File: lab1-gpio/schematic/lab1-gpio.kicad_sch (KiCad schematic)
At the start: 9 parts

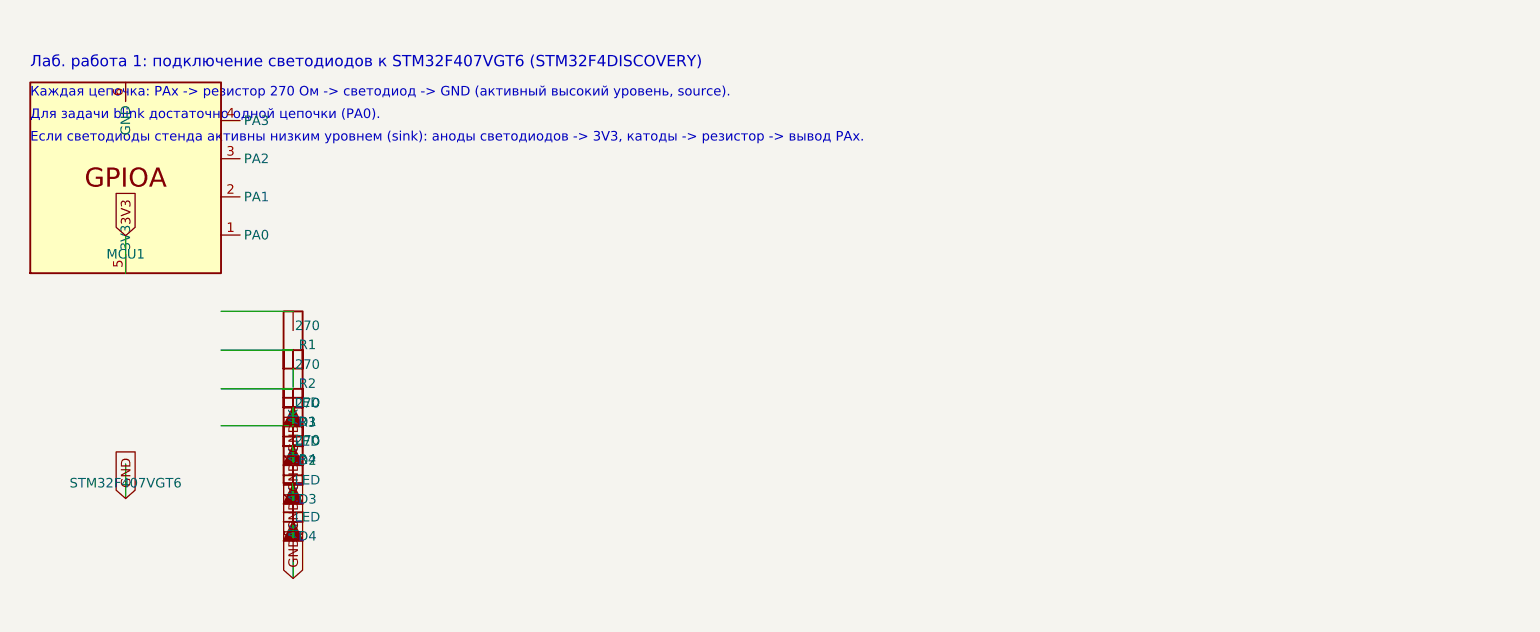
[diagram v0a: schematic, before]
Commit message: Lab 1: fix schema, add validator
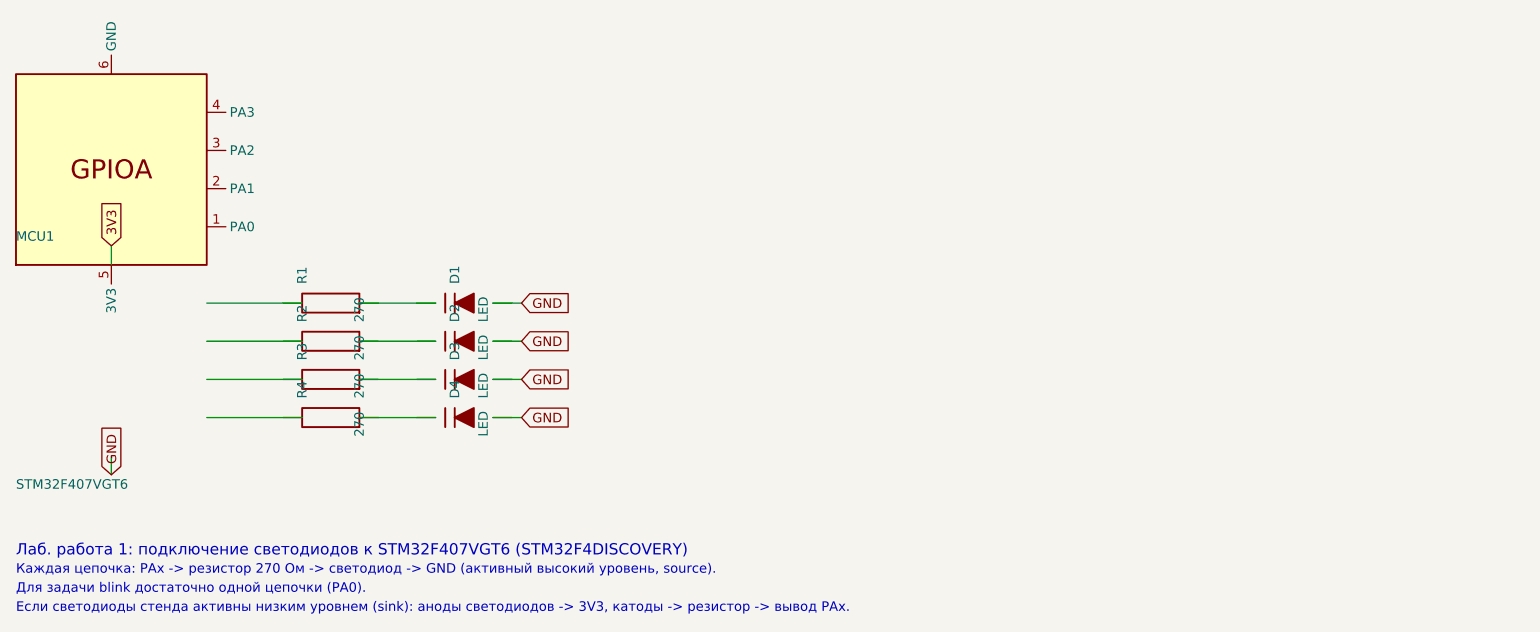
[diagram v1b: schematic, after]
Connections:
- net GND: no longer D4.2 (K), R3.1, R4.1
- net at R1.1: now also D1.2 (K)
- net at R2.1: now also D2.2 (K); no longer R4.2
- net at D3.2 (K): now also R3.1
- new net: D4.2 (K), R4.1
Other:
- moved on the sheet: MCU1, R1, R2, R3, R4
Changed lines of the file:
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@@
     (title "Лаб. работа 1: подключение светодиодов к STM32F407VGT6")
     (date "2026-09-12")
-    (rev "1.0")
+    (rev "1.1")
   )
-  ; ============ MCU ============
-  (symbol (lib_id "Lab:STM32F407_GPIO") (at 40 90 0)
+  (symbol (lib_id "Lab:STM32F407_GPIO") (at 38.1 88.9 0)
     (unit 1)
     (in_bom yes) (on_board yes)
-    (property "Reference" "MCU1" (at 52.7 87.46 0) (effects (font (size 1.27 1.27))))
-    (property "Value" "STM32F407VGT6" (at 52.7 117.94 0) (effects (font (size 1.27 1.27))))
+    (property "Reference" "MCU1" (at 38.1 85.09 0) (effects (font (size 1.27 1.27)) (justify left)))
+    (property "Value" "STM32F407VGT6" (at 38.1 118.11 0) (effects (font (size 1.27 1.27)) (justify left)))
   )
-  ; ============ Цепочка PA0 ============
-  (wire (pts (xy 65.4 95.08) (xy 75 95.08)) (stroke (width 0) (type default))
+  (wire (pts (xy 50.8 88.9) (xy 50.8 86.36)) (stroke (width 0) (type default))
 )
-  (symbol (lib_id "Lab:R") (at 75 98.89 0)
+  (global_label "3V3" (shape input) (at 50.8 86.36 90)
+    (effects (font (size 1.27 1.27)) (justify left))
+)
+  (wire (pts (xy 50.8 114.3) (xy 50.8 116.84)) (stroke (width 0) (type default))
+)
+  (global_label "GND" (shape input) (at 50.8 116.84 270)
+    (effects (font (size 1.27 1.27)) (justify left))
+)
+  (wire (pts (xy 63.5 93.98) (xy 76.2 93.98)) (stroke (width 0) (type default))
+)
+  (symbol (lib_id "Lab:R") (at 80.01 93.98 90)
     (unit 1)
     (in_bom yes) (on_board yes)
-    (property "Reference" "R1" (at 76.905 99.525 0) (effects (font (size 1.27 1.27))))
-    (property "Value" "270" (at 76.905 96.985 0) (effects (font (size 1.27 1.27))))
+    (property "Reference" "R1" (at 76.2 91.44 0) (effects (font (size 1.27 1.27)) (justify left)))
+    (property "Value" "270" (at 83.82 96.52 0) (effects (font (size 1.27 1.27)) (justify left)))
   )
-  (wire (pts (xy 75 102.7) (xy 75 105.16)) (stroke (width 0) (type default))
+  (wire (pts (xy 83.82 93.98) (xy 93.98 93.98)) (stroke (width 0) (type default))
 )
-  (symbol (lib_id "Lab:LED") (at 75 109.13 0)
+  (symbol (lib_id "Lab:LED") (at 97.79 93.98 90)
     (unit 1)
     (in_bom yes) (on_board yes)
-    (property "Reference" "D1" (at 76.905 109.765 0) (effects (font (size 1.27 1.27))))
-    (property "Value" "LED" (at 76.905 107.225 0) (effects (font (size 1.27 1.27))))
+    (property "Reference" "D1" (at 96.52 91.44 0) (effects (font (size 1.27 1.27)) (justify left)))
+    (property "Value" "LED" (at 100.33 96.52 0) (effects (font (size 1.27 1.27)) (justify left)))
   )
-  (wire (pts (xy 75 112.94) (xy 75 115.4)) (stroke (width 0) (type default))
+  (wire (pts (xy 101.6 93.98) (xy 105.41 93.98)) (stroke (width 0) (type default))
 )
-  (global_label "GND" (shape input) (at 75 115.4 90)
+  (global_label "GND" (shape input) (at 105.41 93.98 0)
     (effects (font (size 1.27 1.27)) (justify left))
 )
-  ; ============ Цепочка PA1 ============
-  (wire (pts (xy 65.4 100.24) (xy 75 100.24)) (stroke (width 0) (type default))
+  (wire (pts (xy 63.5 99.06) (xy 76.2 99.06)) (stroke (width 0) (type default))
 )
-  (symbol (lib_id "Lab:R") (at 75 104.05 0)
+  (symbol (lib_id "Lab:R") (at 80.01 99.06 90)
     (unit 1)
     (in_bom yes) (on_board yes)
-    (property "Reference" "R2" (at 76.905 104.685 0) (effects (font (size 1.27 1.27))))
-    (property "Value" "270" (at 76.905 102.145 0) (effects (font (size 1.27 1.27))))
+    (property "Reference" "R2" (at 76.2 96.52 0) (effects (font (size 1.27 1.27)) (justify left)))
+    (property "Value" "270" (at 83.82 101.6 0) (effects (font (size 1.27 1.27)) (justify left)))
   )
-  (wire (pts (xy 75 107.86) (xy 75 110.32)) (stroke (width 0) (type default))
+  (wire (pts (xy 83.82 99.06) (xy 93.98 99.06)) (stroke (width 0) (type default))
 )
-  (symbol (lib_id "Lab:LED") (at 75 114.29 0)
+  (symbol (lib_id "Lab:LED") (at 97.79 99.06 90)
     (unit 1)
     (in_bom yes) (on_board yes)
-    (property "Reference" "D2" (at 76.905 114.925 0) (effects (font (size 1.27 1.27))))
-    (property "Value" "LED" (at 76.905 112.385 0) (effects (font (size 1.27 1.27))))
+    (property "Reference" "D2" (at 96.52 96.52 0) (effects (font (size 1.27 1.27)) (justify left)))
+    (property "Value" "LED" (at 100.33 101.6 0) (effects (font (size 1.27 1.27)) (justify left)))
   )
-  (wire (pts (xy 75 118.1) (xy 75 120.56)) (stroke (width 0) (type default))
+  (wire (pts (xy 101.6 99.06) (xy 105.41 99.06)) (stroke (width 0) (type default))
 )
-  (global_label "GND" (shape input) (at 75 120.56 90)
+  (global_label "GND" (shape input) (at 105.41 99.06 0)
     (effects (font (size 1.27 1.27)) (justify left))
 )
-  ; ============ Цепочка PA2 ============
-  (wire (pts (xy 65.4 105.4) (xy 75 105.4)) (stroke (width 0) (type default))
+  (wire (pts (xy 63.5 104.14) (xy 76.2 104.14)) (stroke (width 0) (type default))
 )
-  (symbol (lib_id "Lab:R") (at 75 109.21 0)
+  (symbol (lib_id "Lab:R") (at 80.01 104.14 90)
     (unit 1)
     (in_bom yes) (on_board yes)
-    (property "Reference" "R3" (at 76.905 109.845 0) (effects (font (size 1.27 1.27))))
-    (property "Value" "270" (at 76.905 107.305 0) (effects (font (size 1.27 1.27))))
+    (property "Reference" "R3" (at 76.2 101.6 0) (effects (font (size 1.27 1.27)) (justify left)))
+    (property "Value" "270" (at 83.82 106.68 0) (effects (font (size 1.27 1.27)) (justify left)))
   )
-  (wire (pts (xy 75 113.02) (xy 75 115.48)) (stroke (width 0) (type default))
+  (wire (pts (xy 83.82 104.14) (xy 93.98 104.14)) (stroke (width 0) (type default))
 )
-  (symbol (lib_id "Lab:LED") (at 75 119.45 0)
+  (symbol (lib_id "Lab:LED") (at 97.79 104.14 90)
     (unit 1)
     (in_bom yes) (on_board yes)
-    (property "Reference" "D3" (at 76.905 120.085 0) (effects (font (size 1.27 1.27))))
-    (property "Value" "LED" (at 76.905 117.545 0) (effects (font (size 1.27 1.27))))
+    (property "Reference" "D3" (at 96.52 101.6 0) (effects (font (size 1.27 1.27)) (justify left)))
+    (property "Value" "LED" (at 100.33 106.68 0) (effects (font (size 1.27 1.27)) (justify left)))
   )
-  (wire (pts (xy 75 123.26) (xy 75 125.72)) (stroke (width 0) (type default))
+  (wire (pts (xy 101.6 104.14) (xy 105.41 104.14)) (stroke (width 0) (type default))
 )
-  (global_label "GND" (shape input) (at 75 125.72 90)
+  (global_label "GND" (shape input) (at 105.41 104.14 0)
     (effects (font (size 1.27 1.27)) (justify left))
 )
-  ; ============ Цепочка PA3 ============
-  (wire (pts (xy 65.4 110.32) (xy 75 110.32)) (stroke (width 0) (type default))
+  (wire (pts (xy 63.5 109.22) (xy 76.2 109.22)) (stroke (width 0) (type default))
 )
-  (symbol (lib_id "Lab:R") (at 75 114.13 0)
+  (symbol (lib_id "Lab:R") (at 80.01 109.22 90)
     (unit 1)
     (in_bom yes) (on_board yes)
-    (property "Reference" "R4" (at 76.905 114.765 0) (effects (font (size 1.27 1.27))))
-    (property "Value" "270" (at 76.905 112.225 0) (effects (font (size 1.27 1.27))))
+    (property "Reference" "R4" (at 76.2 106.68 0) (effects (font (size 1.27 1.27)) (justify left)))
+    (property "Value" "270" (at 83.82 111.76 0) (effects (font (size 1.27 1.27)) (justify left)))
   )
-  (wire (pts (xy 75 117.94) (xy 75 120.4)) (stroke (width 0) (type default))
+  (wire (pts (xy 83.82 109.22) (xy 93.98 109.22)) (stroke (width 0) (type default))
 )
-  (symbol (lib_id "Lab:LED") (at 75 124.37 0)
+  (symbol (lib_id "Lab:LED") (at 97.79 109.22 90)
     (unit 1)
     (in_bom yes) (on_board yes)
-    (property "Reference" "D4" (at 76.905 125.005 0) (effects (font (size 1.27 1.27))))
-    (property "Value" "LED" (at 76.905 122.465 0) (effects (font (size 1.27 1.27))))
+    (property "Reference" "D4" (at 96.52 106.68 0) (effects (font (size 1.27 1.27)) (justify left)))
+    (property "Value" "LED" (at 100.33 111.76 0) (effects (font (size 1.27 1.27)) (justify left)))
   )
-  (wire (pts (xy 75 128.18) (xy 75 130.64)) (stroke (width 0) (type default))
+  (wire (pts (xy 101.6 109.22) (xy 105.41 109.22)) (stroke (width 0) (type default))
 )
-  (global_label "GND" (shape input) (at 75 130.64 90)
+  (global_label "GND" (shape input) (at 105.41 109.22 0)
     (effects (font (size 1.27 1.27)) (justify left))
 )
-  ; ============ Питание MCU ============
-  (wire (pts (xy 52.7 90) (xy 52.7 85)) (stroke (width 0) (type default))
-)
-  (global_label "3V3" (shape input) (at 52.7 85 90)
-    (effects (font (size 1.27 1.27)) (justify left))
-)
-  (wire (pts (xy 52.7 115.4) (xy 52.7 120)) (stroke (width 0) (type default))
-)
-  (global_label "GND" (shape input) (at 52.7 120 90)
-    (effects (font (size 1.27 1.27)) (justify left))
-)
-  ; ============ Пояснения ============
   (text "Лаб. работа 1: подключение светодиодов к STM32F407VGT6 (STM32F4DISCOVERY)"
-    (at 40 62 0) (effects (font (size 1.5 1.5)) (justify left))
+    (at 38.1 127 0) (effects (font (size 1.5 1.5)) (justify left))
 )
   (text "Каждая цепочка: PAx -> резистор 270 Ом -> светодиод -> GND (активный высокий уровень, source)."
-    (at 40 66 0) (effects (font (size 1.27 1.27)) (justify left))
+    (at 38.1 129.54 0) (effects (font (size 1.27 1.27)) (justify left))
 )
   (text "Для задачи blink достаточно одной цепочки (PA0)."
-    (at 40 69 0) (effects (font (size 1.27 1.27)) (justify left))
+    (at 38.1 132.08 0) (effects (font (size 1.27 1.27)) (justify left))
 )
   (text "Если светодиоды стенда активны низким уровнем (sink): аноды светодиодов -> 3V3, катоды -> резистор -> вывод PAx."
-    (at 40 72 0) (effects (font (size 1.27 1.27)) (justify left))
+    (at 38.1 134.62 0) (effects (font (size 1.27 1.27)) (justify left))
 )
   (sheet_instances

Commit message: Fix lab 1
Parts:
- removed D1, D2, D3, D4: LED, symbol Lab:LED
- removed MCU1: STM32F407VGT6, symbol Lab:STM32F407_GPIO
- removed R1, R2, R3, R4: 270, symbol Lab:R
- added D1, D2, D3, D4: LED, LED_SMD:LED_0805_2012Metric, symbol Device:LED
- added R1, R2, R3, R4: 270, Resistor_SMD:R_0805_2012Metric, symbol Device:R
- added U1: STM32F407VGT6, Package_QFP:LQFP-100_14x14mm_P0.5mm, symbol MCU_ST_STM32F4:STM32F407VGTx
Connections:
- net GND: now also D1.1 (K), D2.1 (K), D3.1 (K), D4.1 (K), U1.10 (VSS), U1.20 (VSSA), U1.27 (VSS), U1.74 (VSS), U1.99 (VSS)
- new net: D1.2 (A), R1.2
- new net: D2.2 (A), R2.2
- new net: D4.2 (A), R4.2
- new net: D3.2 (A), R3.2
- new net +3V3: U1.100 (VDD), U1.11 (VDD), U1.19 (VDD), U1.22 (VDDA), U1.28 (VDD), U1.50 (VDD), U1.6 (VBAT), U1.75 (VDD)
- new net PA0: R1.1, U1.23 (PA0)
- new net PA1: R2.1, U1.24 (PA1)
- new net PA2: R3.1, U1.25 (PA2)
- new net PA3: R4.1, U1.26 (PA3)
- no-connect marks 0 -> 83
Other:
- note added: "Каждая цепочка: PAx -> резистор 270 Ом -> светодиод (анод к резистору) -> GND; активный высокий уровень (source)."
- note added: "Лабораторная работа #1: подключение светодиодов к STM32F407VGT6 (STM32F4DISCOVERY)"
- note added: "Светодиоды управляются выводами PA0–PA3 порта GPIOA (бегущий огонь)."
- note removed: "Для задачи blink достаточно одной цепочки (PA0)."
- note removed: "Если светодиоды стенда активны низким уровнем (sink): аноды светодиодов -> 3V3, катоды -> резистор -> вывод PAx."
- note removed: "Каждая цепочка: PAx -> резистор 270 Ом -> светодиод -> GND (активный высокий уровень, source)."
- note removed: "Лаб. работа 1: подключение светодиодов к STM32F407VGT6 (STM32F4DISCOVERY)"
- title: Лаб. работа 1: подключение светодиодов к STM32F407VGT6 -> (none)
